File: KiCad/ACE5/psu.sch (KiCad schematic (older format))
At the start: 31 parts, among them IC1 LM7805_TO220

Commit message: Address inconsistencies between 3,4,5. Renumber part to reflect version. Relocate Z80 parts library to separate repository.
https://github.com/flypie/Z80-CPU-for-KiCAD

Signed-off-by: John Bradley <flypie@rocketmail.com>
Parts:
- removed Z10, Z11, Z9: 74AHCT393, Package_DIP:DIP-14_W7.62mm, symbol 74xx:74LS393
- removed Z19: 74AHCT00, Package_DIP:DIP-14_W7.62mm, symbol 74xx:74LS00
- removed Z25: 74AHCT02, Package_DIP:DIP-14_W7.62mm, symbol 74xx:74LS02
- POWER-9V-DC1: footprint cuipj:CUI_PJ-036C -> SamacSys_Parts:163179PHEX; symbol Connector_Generic:Conn_01x02 -> SamacSys_Parts:163-179PH-EX
- Z100: footprint Package_DIP:DIP-16_W7.62mm -> Package_DIP:DIP-16_W7.62mm_Socket
- Z102, Z20, Z21, Z22, Z23, Z24, Z27: footprint Package_DIP:DIP-14_W7.62mm -> Package_DIP:DIP-14_W7.62mm_Socket
- renumbered C12 to C10, C13 to C11, C14 to C12, C15 to C13, C16 to C14, C17 to C15, C18 to C16, C19 to C17, C20 to C18, C21 to C19, C9 to C4, C10 to C8, C11 to C9
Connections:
- wire segments 105 -> 95
- no-connect marks 0 -> 1

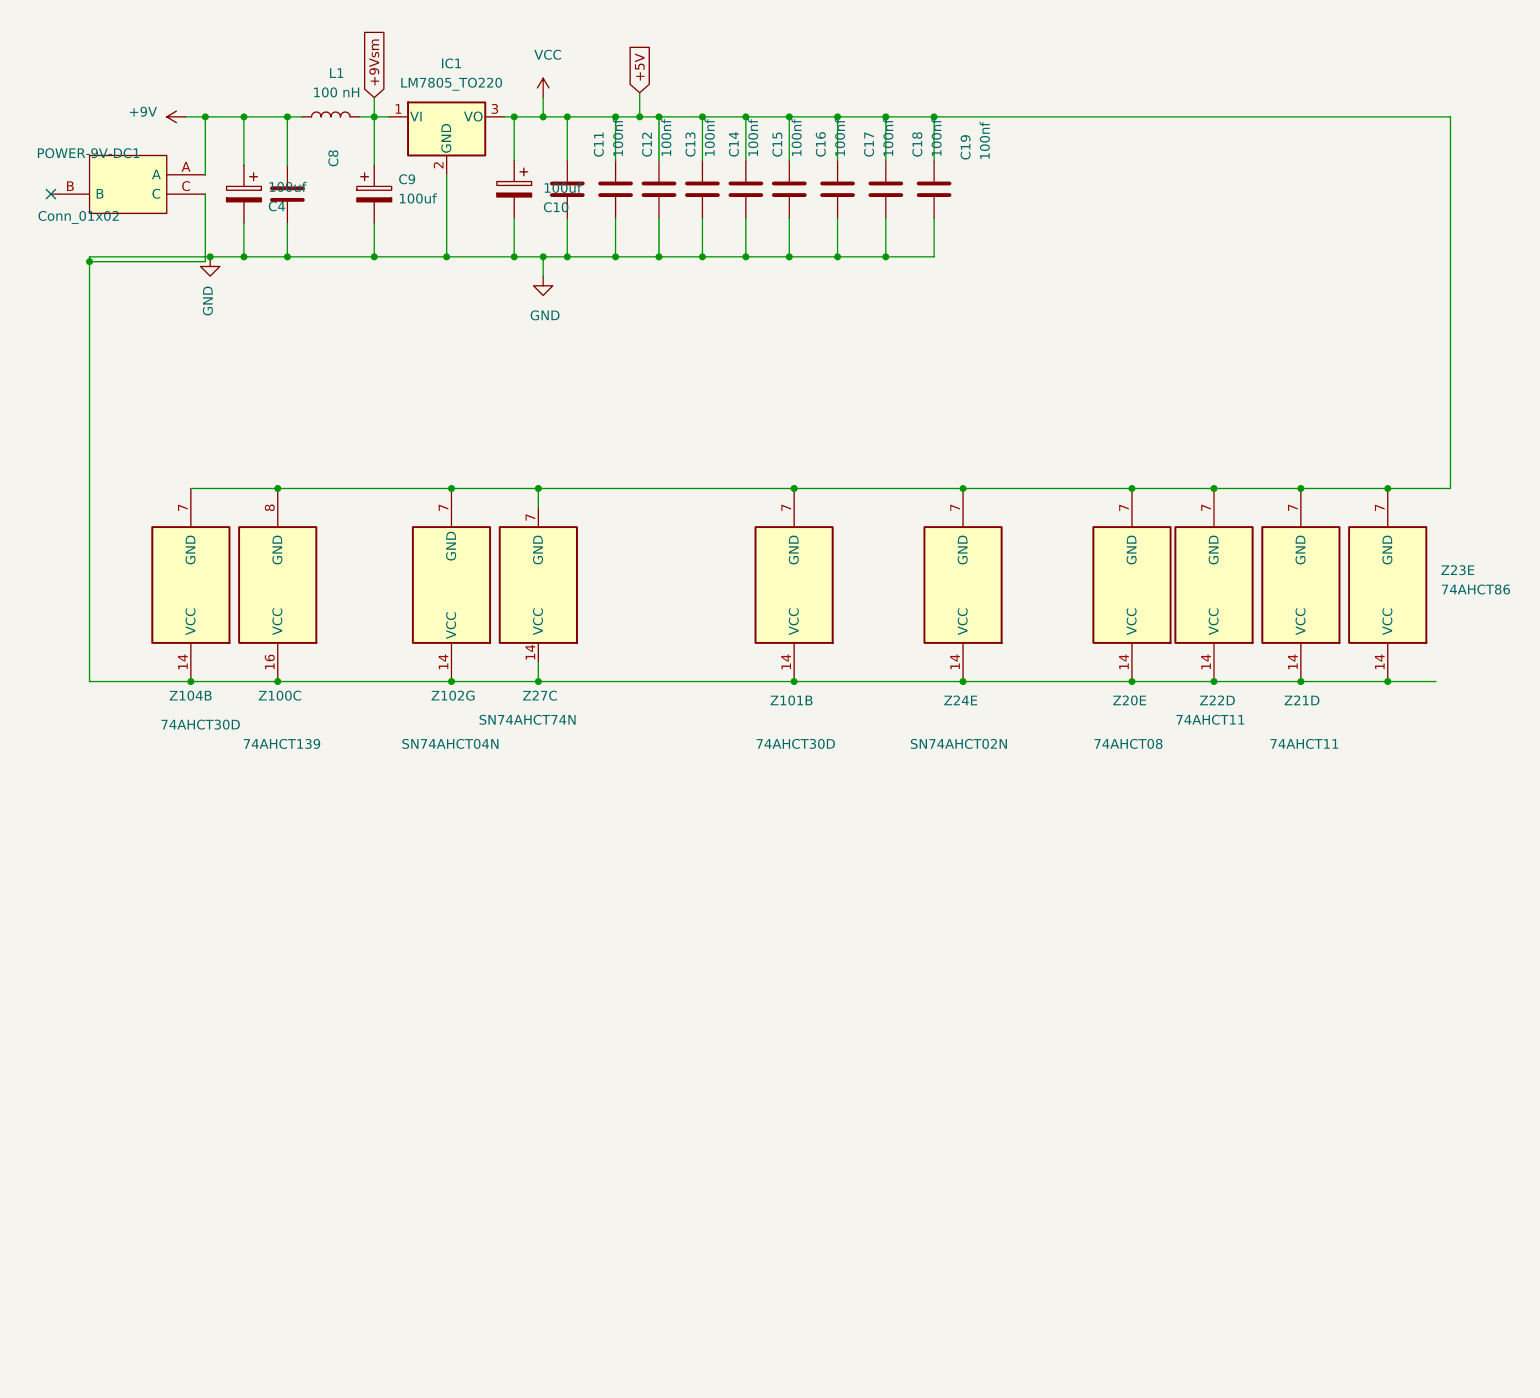
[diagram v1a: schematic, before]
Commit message: Rearrange boards 4 & 5. Make IC numbering consistent.
Signed-off-by: John Bradley <flypie@rocketmail.com>
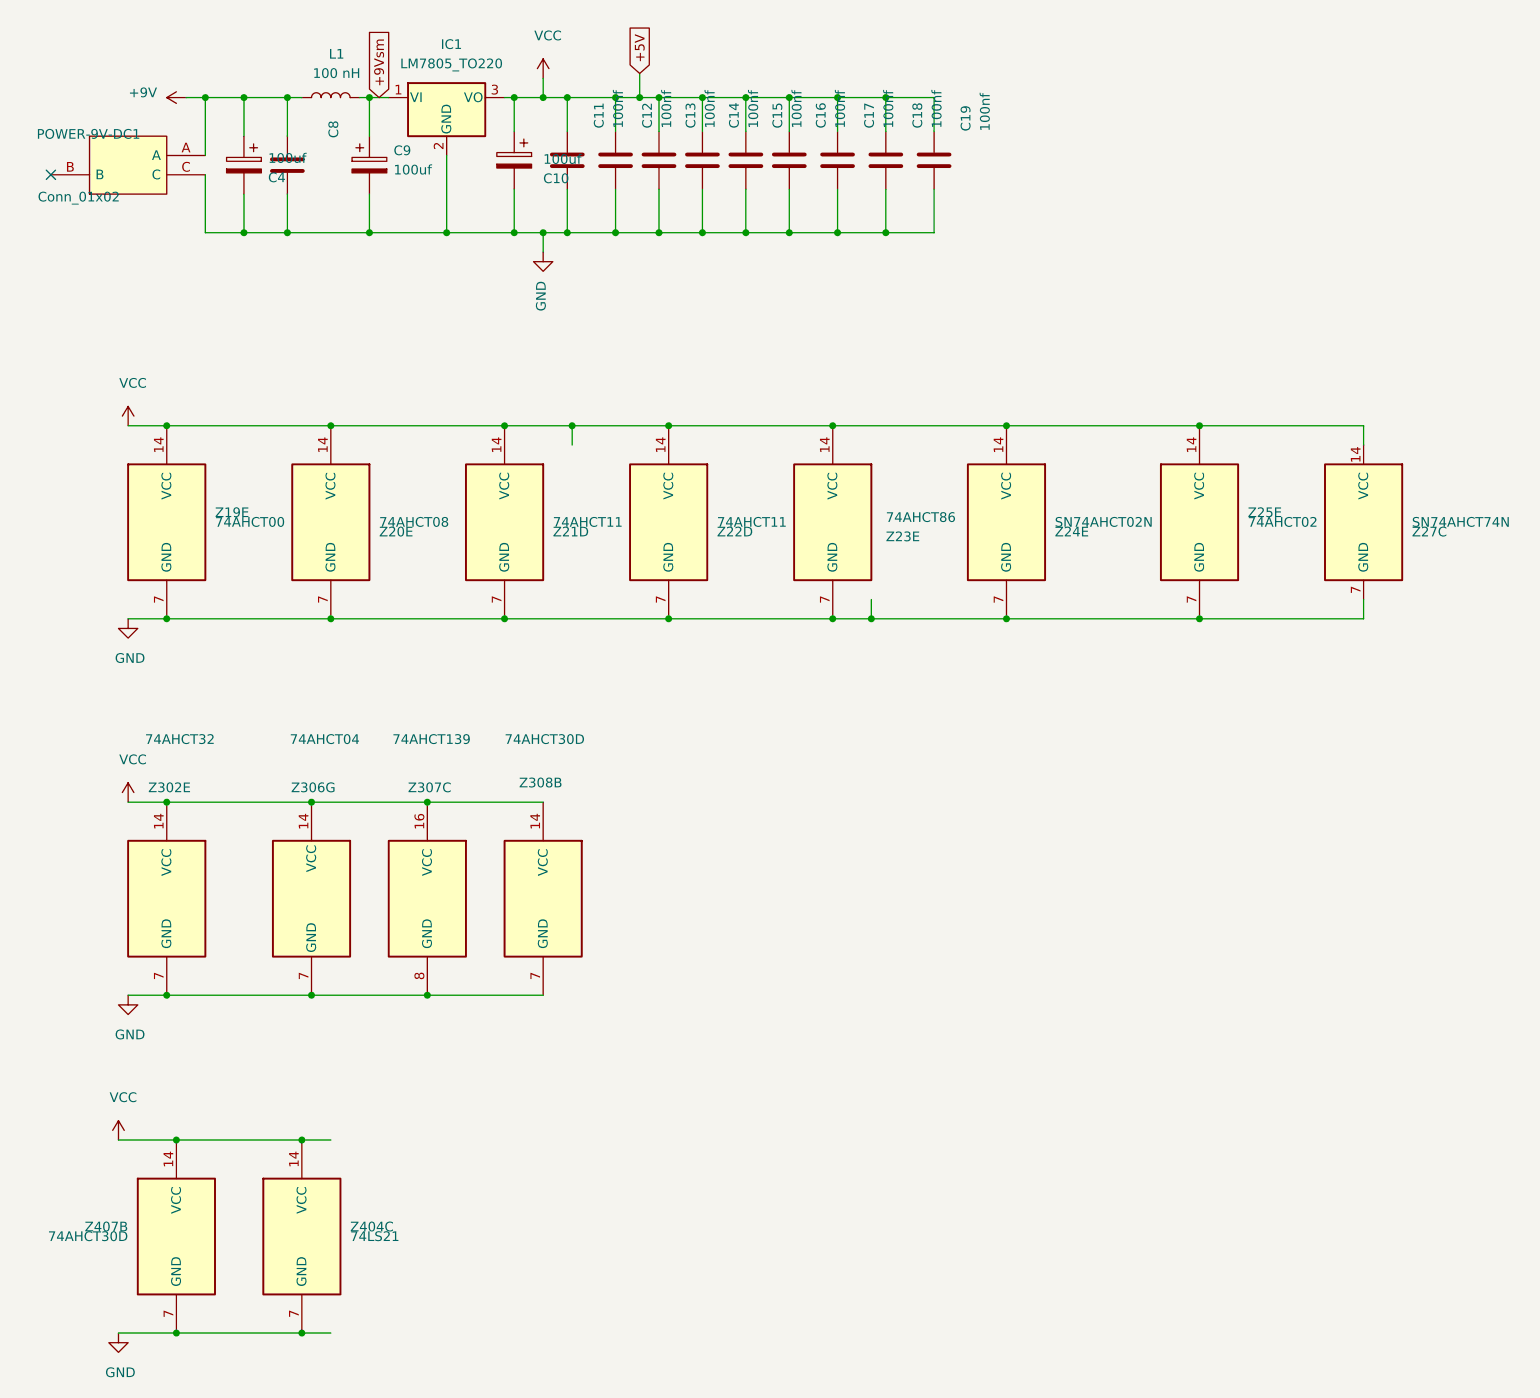
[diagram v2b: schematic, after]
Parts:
- removed Z104: 74AHCT30D, Package_SO:SOIC-14_3.9x8.7mm_P1.27mm, symbol 74xx:74LS30
- added Z19: 74AHCT00, Package_DIP:DIP-14_W7.62mm_Socket, symbol 74xx:74LS00
- added Z25: 74AHCT02, Package_DIP:DIP-14_W7.62mm_Socket, symbol 74xx:74HCT02
- added Z302: 74AHCT32, Package_DIP:DIP-14_W7.62mm_Socket, symbol 74xx:74LS32
- added Z404: 74LS21, Package_DIP:DIP-14_W7.62mm_Socket, symbol 74xx:74LS21
- added Z407: 74AHCT30D, Package_SO:SOIC-14_3.9x8.7mm_P1.27mm, symbol 74xx:74LS30
- Z306: renamed from Z102; value SN74AHCT04N -> 74AHCT04
- renumbered Z100 to Z307, Z101 to Z308
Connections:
- wire segments 95 -> 101
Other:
- moved on the sheet: C10, C11, C12, C13, C14, C15, C16, C17, C18, C19, C4, C8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

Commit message: Update ACE3NOKB to reflect errors in Mem Decode. ACE5NOKB test SMT ideas. Added 180 & 380.
Signed-off-by: John Bradley <flypie@rocketmail.com>
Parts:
- removed Z23: 74AHCT86, Package_DIP:DIP-14_W7.62mm_Socket, symbol 74xx:74LS86
- C10, C4: footprint Capacitor_THT:CP_Radial_D5.0mm_P2.00mm -> Capacitor_SMD:CP_Elec_6.3x5.3
- C11, C12, C13, C14, C15, C16, C17, C18, C19, C8: footprint Capacitor_THT:C_Disc_D3.0mm_W1.6mm_P2.50mm -> Capacitor_SMD:C_1206_3216Metric
- C9: footprint Capacitor_THT:CP_Radial_D4.0mm_P1.50mm -> Capacitor_SMD:CP_Elec_6.3x5.3
- IC1: value LM7805_TO220 -> LM7805MPX_NOPB; footprint Package_TO_SOT_THT:TO-220-3_Vertical -> Package_TO_SOT_SMD:SOT-223; symbol Regulator_Linear:LM7805_TO220 -> SamacSys_Parts:LM7805MPX_NOPB; Description (none) -> Linear Voltage Regulators 1.5-A, Wide VIN Fixed Voltage Reg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; Height (none) -> 1.8; Manufacturer_Name (none) -> Texas Instruments; Manufacturer_Part_Number (none) -> LM7805MPX/NOPB; Mouser Part Number (none) -> 595-LM7805MPX/NOPB; Mouser Price/Stock (none) -> https://www.mouser.co.uk/ProductDetail/Texas-Instruments/LM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
- L1: footprint SamacSys_Parts:KEMET_SBT_0260T -> Inductor_SMD:L_1812_4532Metric_Pad1.30x3.40mm_HandSolder
- POWER-9V-DC1: footprint SamacSys_Parts:163179PHEX -> Connector_BarrelJack:BarrelJack_CUI_PJ-036AH-SMT_Horizontal; symbol SamacSys_Parts:163-179PH-EX -> SamacSys_Parts:PJ-036AH-SMT-TR
- Z19: value 74AHCT00 -> 74AHCT2G00; footprint Package_DIP:DIP-14_W7.62mm_Socket -> Package_SO:TSSOP-8_3x3mm_P0.65mm; symbol 74xx:74LS00 -> ExtraSymbols:74AHCT2G00
- Z20, Z21, Z22, Z24, Z25, Z27, Z302, Z404: footprint Package_DIP:DIP-14_W7.62mm_Socket -> Package_SO:SOIC-14_3.9x8.7mm_P1.27mm
- Z306: footprint Package_DIP:DIP-14_W7.62mm_Socket -> Package_SO:SOIC-16_3.9x9.9mm_P1.27mm
- Z307: footprint Package_DIP:DIP-16_W7.62mm_Socket -> Package_SO:SOIC-16_3.9x9.9mm_P1.27mm
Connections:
- wire segments 101 -> 97
